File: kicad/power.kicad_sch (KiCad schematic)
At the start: 18 parts, among them J13 USB4125-GF-A, SW1 ANT11TFHQE, SW2 E112SD1A3QE, U40 MCP1700-3302E/TO, X1 25.175 MHz

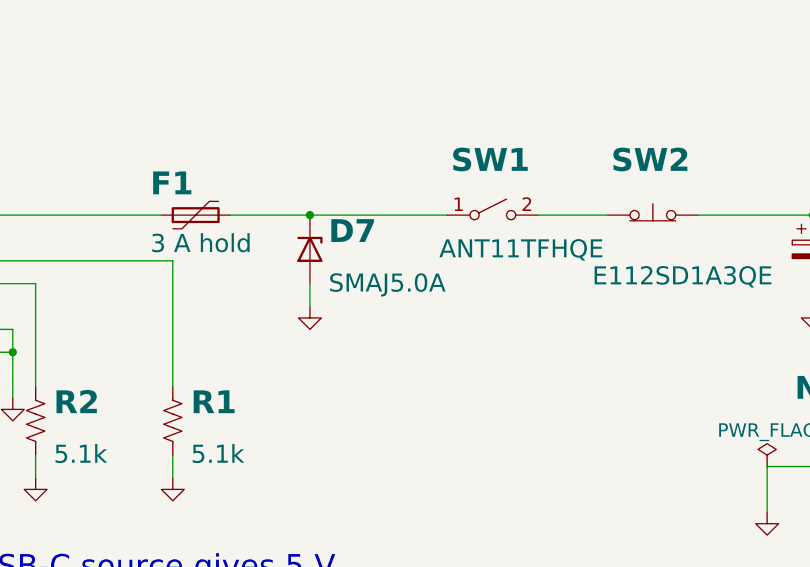
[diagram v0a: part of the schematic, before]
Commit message: Through-hole ESD clamps on external I/O; D7 TVS to through-hole SA5.0A
BAT85 steering pairs to +5V and GND on every PS/2 and SNES signal line
(D8-D21, shared port sheet) and on the VGA syncs (D22-D25, video sheet).
D7 changes from the SMD SMAJ5.0A to the DO-15 SA5.0A (through hole
wherever possible). BOM, docs and PDFs regenerated.

Co-Authored-By: Claude Opus 5.5 (1M context) <noreply@anthropic.com>
Claude-Session: https://claude.ai/code/session_01L9AkLuEg13EebxDmgXsaEp
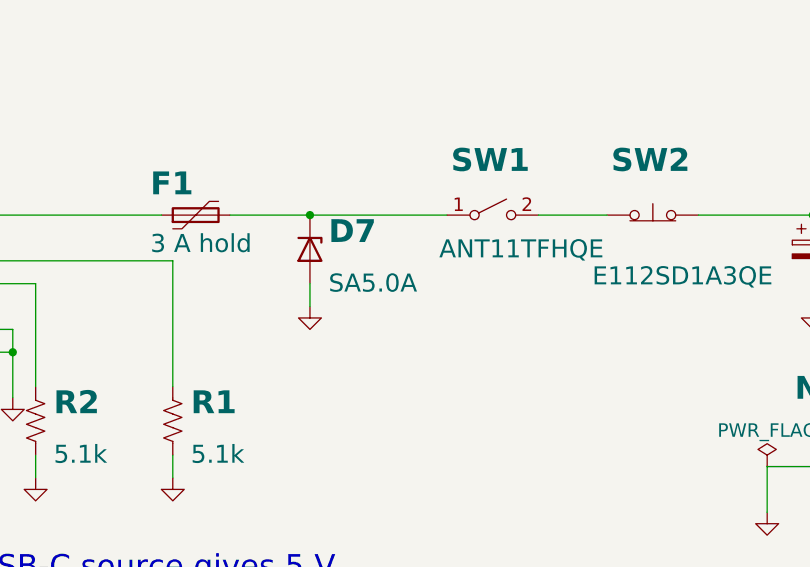
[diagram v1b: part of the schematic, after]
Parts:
- D7: value SMAJ5.0A -> SA5.0A; footprint Diode_SMD:D_SMA -> Diode_THT:D_DO-15_P10.16mm_Horizontal; MPN SMAJ5.0A -> SA5.0A
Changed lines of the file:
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@@
   (wire (pts (xy 104.14 88.9) (xy 104.14 91.44)) (stroke (width 0) (type default)))
   (symbol (lib_id "power:GND") (at 104.14 91.44 0) (unit 1) (in_bom yes) (on_board yes) (dnp no) (property "Reference" "#PWR0202" (at 104.14 91.44 0) (effects (font (size 1.27 1.27)) hide)) (property "Value" "GND" (at 104.14 97.79 0) (effects (font (size 2 2)) hide)) (property "Footprint" "" (at 104.14 91.44 0) (effects (font (size 1.27 1.27)) hide)) (property "Datasheet" "" (at 104.14 91.44 0) (effects (font (size 1.27 1.27)) hide)) (pin "1") (instances (project "placard" (path "/e3450542-4ffc-59d4-a4a7-45636233928a/f2696644-57a6-5352-a354-a3e1bf43cc65" (reference "#PWR0202") (unit 1)))))
-  (symbol (lib_id "placard_std:D_Zener") (at 104.14 85.09 270) (unit 1) (in_bom yes) (on_board yes) (dnp no) (property "Reference" "D7" (at 106.2 84.58 90) (effects (font (size 2.54 2.54) bold) (justify left bottom))) (property "Value" "SMAJ5.0A" (at 106.2 87.68 90) (effects (font (size 2 2)) (justify left top))) (property "Footprint" "Diode_SMD:D_SMA" (at 104.14 85.09 0) (effects (font (size 1.27 1.27)) hide)) (property "Datasheet" "~" (at 104.14 85.09 0) (effects (font (size 1.27 1.27)) hide)) (property "Manufacturer" "Littelfuse" (at 104.14 85.09 0) (effects (font (size 1.27 1.27)) hide)) (property "MPN" "SMAJ5.0A" (at 104.14 85.09 0) (effects (font (size 1.27 1.27)) hide)) (pin "1") (pin "2") (instances (project "placard" (path "/e3450542-4ffc-59d4-a4a7-45636233928a/f2696644-57a6-5352-a354-a3e1bf43cc65" (reference "D7") (unit 1)))))
+  (symbol (lib_id "placard_std:D_Zener") (at 104.14 85.09 270) (unit 1) (in_bom yes) (on_board yes) (dnp no) (property "Reference" "D7" (at 106.2 84.58 90) (effects (font (size 2.54 2.54) bold) (justify left bottom))) (property "Value" "SA5.0A" (at 106.2 87.68 90) (effects (font (size 2 2)) (justify left top))) (property "Footprint" "Diode_THT:D_DO-15_P10.16mm_Horizontal" (at 104.14 85.09 0) (effects (font (size 1.27 1.27)) hide)) (property "Datasheet" "~" (at 104.14 85.09 0) (effects (font (size 1.27 1.27)) hide)) (property "Manufacturer" "Littelfuse" (at 104.14 85.09 0) (effects (font (size 1.27 1.27)) hide)) (property "MPN" "SA5.0A" (at 104.14 85.09 0) (effects (font (size 1.27 1.27)) hide)) (pin "1") (pin "2") (instances (project "placard" (path "/e3450542-4ffc-59d4-a4a7-45636233928a/f2696644-57a6-5352-a354-a3e1bf43cc65" (reference "D7") (unit 1)))))
   (wire (pts (xy 95.25 81.28) (xy 104.14 81.28)) (stroke (width 0) (type default)))
   (wire (pts (xy 104.14 81.28) (xy 119.38 81.28)) (stroke (width 0) (type default)))

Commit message: Part numbers for the remaining parts; J6 Tensility 54-00174; optional J1 and J9-J12
Every schematic part gets Manufacturer/MPN: Yageo MFR-25 resistors by value,
Bourns 4609X networks, KEMET/TDK ceramics, Panasonic FR electrolytics, ECS
oscillator, Assmann VGA, Sullins headers, Wurth box header, Cherry switches.
Sockets get On Shore numbers (0.3" 24/28-pin are ED241DT/ED281DT; ED28DT is
0.6"). J6 becomes the Tensility 54-00174 TRRS jack with a footprint drawn
from its datasheet. Digi-Key prices from Justin for the oscillator, VGA and
audio jack. The expansion slot sockets and the keyboard header are optional,
with a BOM total without them.

Co-Authored-By: Claude Opus 5.5 (1M context) <noreply@anthropic.com>
Claude-Session: https://claude.ai/code/session_01L9AkLuEg13EebxDmgXsaEp
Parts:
- C40, C42: MPN (none) -> C330C105K5R5TA; Manufacturer (none) -> KEMET
- C41: MPN (none) -> EEU-FR1E221; Manufacturer (none) -> Panasonic
- C43: MPN (none) -> C320C104K5R5TA; Manufacturer (none) -> KEMET
- JP1, JP2: MPN (none) -> PREC002SAAN-RC; Manufacturer (none) -> Sullins
- R1, R2: MPN (none) -> MFR-25FBF52-5K1; Manufacturer (none) -> Yageo
- R3, R4: MPN (none) -> MFR-25FBF52-10K; Manufacturer (none) -> Yageo
- X1: MPN (none) -> ECS-100A-251.7; Manufacturer (none) -> ECS Inc.

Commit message: Reset via relay: K1 G5LE-1 NC contact carries 5 V, tactile SW2 drives the coil
SW2 (C&K PTS645VL58-2 LFS) pulls in K1 (Omron G5LE-1 DC5) from VON, so
holding it opens the 5 V line; D26 (BAT85) across the coil. Replaces the
4 A E112SD1A3QE (about $11 -> $2). C41 moves ahead of K1 onto VON so the
board side drains faster on reset. Footprint, layout, BOM and docs updated.

Co-Authored-By: Claude Opus 5.5 (1M context) <noreply@anthropic.com>
Claude-Session: https://claude.ai/code/session_01L9AkLuEg13EebxDmgXsaEp
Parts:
- removed SW2: E112SD1A3QE, placard:SW_Push_CK_E112SD1A3QE, symbol placard_std:SW_Push_Open
- added D26: BAT85, Diode_THT:D_DO-35_SOD27_P7.62mm_Horizontal, symbol placard_std:D_Schottky
- added K1: G5LE-1 DC5, Relay_THT:Relay_SPDT_Omron-G5LE-1, symbol placard_std:G5LE-1
- added SW2: PTS645VL58-2 LFS, Button_Switch_THT:SW_Tactile_SPST_Angled_PTS645Vx58-2LFS, symbol placard_std:SW_Push
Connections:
- net +5V: now also K1.4; no longer C41.1
- net GND: now also D26.2 (A), K1.5
- net at SW1.2 (B): now also C41.1, K1.1, SW2.1
- new net: D26.1 (K), K1.2, SW2.2
- no-connect marks 0 -> 1
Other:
- note added: "one throw. SW2 reset: holding it pulls in K1,"
- note added: "whose NC contact opens the 5 V line."
- note removed: "one throw. SW2 reset: momentary, common + NC,"
- note removed: "so holding it cuts the power."

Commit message: J13: USB4125 footprint with longer SMD pads for hand soldering
New placard:USB_C_Receptacle_GCT_USB4125_6P_HandSolder, made by
gen_kicad_connectors.py from KiCad's USB4125 footprint with the six SMD
pads lengthened 1.5 mm away from the board edge (inner ends unchanged),
so the iron has room to touch each pad. Symbol, power sheet and board
now use it; board drawings regenerated.

Co-Authored-By: Claude Opus 5.5 (1M context) <noreply@anthropic.com>
Claude-Session: https://claude.ai/code/session_01SPs5Hx9ixxAAqtEGqiE4Ba
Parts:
- J13: footprint Connector_USB:USB_C_Receptacle_GCT_USB4125-xx-x_6P_TopMnt_Horizontal -> placard:USB_C_Receptacle_GCT_USB4125_6P_HandSolder
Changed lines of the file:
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@@
   (text "Power and clock" (at 15 22 0) (effects (font (size 6 6) bold) (justify left bottom)))
   (text "USB-C 5 V in, 3.3 V for the SD card, 25.175 MHz oscillator (CLK), cartridge STALL and RUN" (at 15 30 0) (effects (font (size 3 3)) (justify left bottom)))
-  (symbol (lib_id "placard_parts:USB_C_Power") (at 50.8 88.9 0) (unit 1) (in_bom yes) (on_board yes) (dnp no) (property "Reference" "J13" (at 36 75 0) (effects (font (size 2.54 2.54) bold) (justify left bottom))) (property "Value" "USB4125-GF-A" (at 36 104 0) (effects (font (size 2 2)) (justify left top))) (property "Footprint" "Connector_USB:USB_C_Receptacle_GCT_USB4125-xx-x_6P_TopMnt_Horizontal" (at 50.8 88.9 0) (effects (font (size 1.27 1.27)) hide)) (property "Datasheet" "~" (at 50.8 88.9 0) (effects (font (size 1.27 1.27)) hide)) (property "Manufacturer" "GCT" (at 50.8 88.9 0) (effects (font (size 1.27 1.27)) hide)) (property "MPN" "USB4125-GF-A" (at 50.8 88.9 0) (effects (font (size 1.27 1.27)) hide)) (pin "A9") (pin "B9") (pin "A5") (pin "B5") (pin "A12") (pin "B12") (pin "S1") (instances (project "placard" (path "/e3450542-4ffc-59d4-a4a7-45636233928a/f2696644-57a6-5352-a354-a3e1bf43cc65" (reference "J13") (unit 1)))))
+  (symbol (lib_id "placard_parts:USB_C_Power") (at 50.8 88.9 0) (unit 1) (in_bom yes) (on_board yes) (dnp no) (property "Reference" "J13" (at 36 75 0) (effects (font (size 2.54 2.54) bold) (justify left bottom))) (property "Value" "USB4125-GF-A" (at 36 104 0) (effects (font (size 2 2)) (justify left top))) (property "Footprint" "placard:USB_C_Receptacle_GCT_USB4125_6P_HandSolder" (at 50.8 88.9 0) (effects (font (size 1.27 1.27)) hide)) (property "Datasheet" "~" (at 50.8 88.9 0) (effects (font (size 1.27 1.27)) hide)) (property "Manufacturer" "GCT" (at 50.8 88.9 0) (effects (font (size 1.27 1.27)) hide)) (property "MPN" "USB4125-GF-A" (at 50.8 88.9 0) (effects (font (size 1.27 1.27)) hide)) (pin "A9") (pin "B9") (pin "A5") (pin "B5") (pin "A12") (pin "B12") (pin "S1") (instances (project "placard" (path "/e3450542-4ffc-59d4-a4a7-45636233928a/f2696644-57a6-5352-a354-a3e1bf43cc65" (reference "J13") (unit 1)))))
   (wire (pts (xy 68.58 93.98) (xy 71.12 93.98)) (stroke (width 0) (type default)))
   (wire (pts (xy 71.12 93.98) (xy 71.12 96.52)) (stroke (width 0) (type default)))

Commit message: Kit footprints: DIP sockets with puller room and part number, resistors with value
Justin: put the chip-puller room in the socket footprints (User.Eco1,
2.5 mm past each end) and the part number in silkscreen between the pin
rows; resistors get their value in silkscreen on the body. New
gen_kicad_kit_footprints.py derives them from KiCad's stock footprints;
schematic, symbols, BOM and PDFs now name them. The board file is left
as is (Justin is editing it): Update PCB from Schematic swaps them in.

Co-Authored-By: Claude Opus 5.5 (1M context) <noreply@anthropic.com>
Claude-Session: https://claude.ai/code/session_01JnVuvUvdWezUUU6Sgmg16H
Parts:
- R1, R2, R3, R4: footprint Resistor_THT:R_Axial_DIN0207_L6.3mm_D2.5mm_P10.16mm_Horizontal -> placard:R_Axial_DIN0207_L6.3mm_D2.5mm_P10.16mm_Horizontal_Value

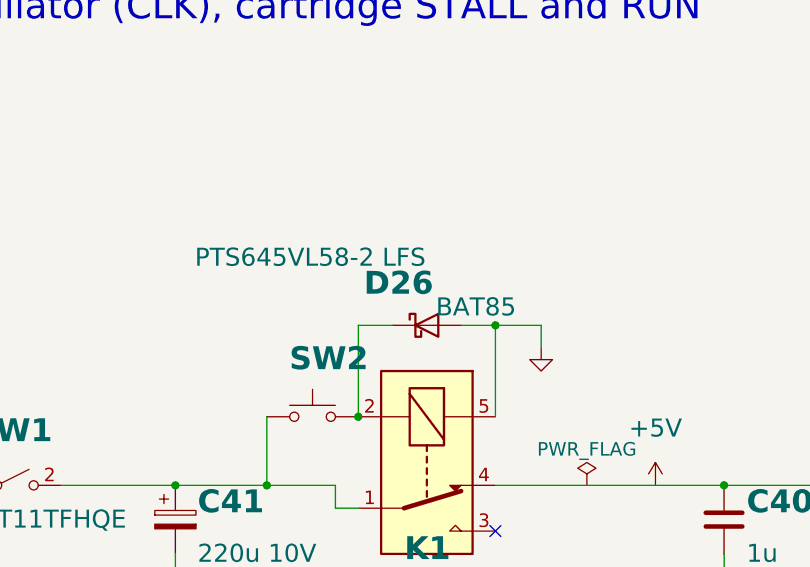
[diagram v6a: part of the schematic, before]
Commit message: Remove the ESD clamps from PS/2, SNES and VGA
Justin decided to take the BAT85 steering pairs out entirely: D8-D21
(shared port sheet) and D22-D25 (video sheet sync lines), 18 diodes.
D7 (TVS on VBUS) stays.

The remaining diodes are renumbered so every kind is numbered from 1 with
no gaps: D26 -> D8 (relay coil), D27-D29 -> D9-D11 (tint BAT85),
D30-D35 -> D12-D17 (tint 1N4148).

The schematic generator now keeps each symbol's uuid from the files
already on disk (and RENUMBERED carries a renamed part's old uuid for one
run), so Update PCB from Schematic renames the renumbered footprints and
leaves every other footprint linked.  kicad/placard.kicad_pcb is not
touched.  BOM, PDFs (no bookmarks panel), placement lists and docs updated.

Co-Authored-By: Claude Opus 5.5 (1M context) <noreply@anthropic.com>
Claude-Session: https://claude.ai/code/session_01DRvpu48w1PN7avX3eFSFuQ
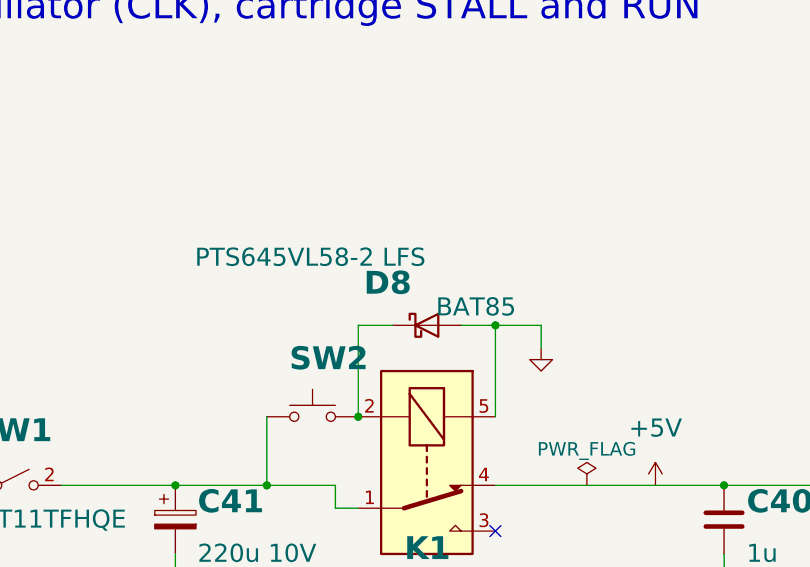
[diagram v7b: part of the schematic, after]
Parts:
- renumbered D26 to D8
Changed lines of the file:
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@@
   (symbol (lib_id "placard_std:G5LE-1") (at 170.18 78.74 270) (unit 1) (in_bom yes) (on_board yes) (dnp no) (property "Reference" "K1" (at 167.68 89.78 90) (effects (font (size 2.54 2.54) bold) (justify left bottom))) (property "Value" "G5LE-1 DC5" (at 167.68 92.28 90) (effects (font (size 2 2)) (justify left top))) (property "Footprint" "Relay_THT:Relay_SPDT_Omron-G5LE-1" (at 170.18 78.74 0) (effects (font (size 1.27 1.27)) hide)) (property "Datasheet" "http://www.omron.com/ecb/products/pdf/en-g5le.pdf" (at 170.18 78.74 0) (effects (font (size 1.27 1.27)) hide)) (property "Manufacturer" "Omron" (at 170.18 78.74 0) (effects (font (size 1.27 1.27)) hide)) (property "MPN" "G5LE-1 DC5" (at 170.18 78.74 0) (effects (font (size 1.27 1.27)) hide)) (pin "1") (pin "2") (pin "3") (pin "4") (pin "5") (instances (project "placard" (path "/e3450542-4ffc-59d4-a4a7-45636233928a/f2696644-57a6-5352-a354-a3e1bf43cc65" (reference "K1") (unit 1)))))
   (symbol (lib_id "placard_std:SW_Push") (at 157.48 73.66 0) (unit 1) (in_bom yes) (on_board yes) (dnp no) (property "Reference" "SW2" (at 154.9 68.68 0) (effects (font (size 2.54 2.54) bold) (justify left bottom))) (property "Value" "PTS645VL58-2 LFS" (at 144.4 54.78 0) (effects (font (size 2 2)) (justify left top))) (property "Footprint" "Button_Switch_THT:SW_Tactile_SPST_Angled_PTS645Vx58-2LFS" (at 157.48 73.66 0) (effects (font (size 1.27 1.27)) hide)) (property "Datasheet" "~" (at 157.48 73.66 0) (effects (font (size 1.27 1.27)) hide)) (property "Manufacturer" "C&K" (at 157.48 73.66 0) (effects (font (size 1.27 1.27)) hide)) (property "MPN" "PTS645VL58-2 LFS" (at 157.48 73.66 0) (effects (font (size 1.27 1.27)) hide)) (pin "1") (pin "2") (instances (project "placard" (path "/e3450542-4ffc-59d4-a4a7-45636233928a/f2696644-57a6-5352-a354-a3e1bf43cc65" (reference "SW2") (unit 1)))))
-  (symbol (lib_id "placard_std:D_Schottky") (at 170.18 63.5 0) (unit 1) (in_bom yes) (on_board yes) (dnp no) (property "Reference" "D26" (at 163.18 60.3 0) (effects (font (size 2.54 2.54) bold) (justify left bottom))) (property "Value" "BAT85" (at 171.18 60.3 0) (effects (font (size 2 2)) (justify left top))) (property "Footprint" "Diode_THT:D_DO-35_SOD27_P7.62mm_Horizontal" (at 170.18 63.5 0) (effects (font (size 1.27 1.27)) hide)) (property "Datasheet" "~" (at 170.18 63.5 0) (effects (font (size 1.27 1.27)) hide)) (property "Manufacturer" "Vishay" (at 170.18 63.5 0) (effects (font (size 1.27 1.27)) hide)) (property "MPN" "BAT85" (at 170.18 63.5 0) (effects (font (size 1.27 1.27)) hide)) (pin "1") (pin "2") (instances (project "placard" (path "/e3450542-4ffc-59d4-a4a7-45636233928a/f2696644-57a6-5352-a354-a3e1bf43cc65" (reference "D26") (unit 1)))))
+  (symbol (lib_id "placard_std:D_Schottky") (at 170.18 63.5 0) (unit 1) (in_bom yes) (on_board yes) (dnp no) (property "Reference" "D8" (at 163.18 60.3 0) (effects (font (size 2.54 2.54) bold) (justify left bottom))) (property "Value" "BAT85" (at 171.18 60.3 0) (effects (font (size 2 2)) (justify left top))) (property "Footprint" "Diode_THT:D_DO-35_SOD27_P7.62mm_Horizontal" (at 170.18 63.5 0) (effects (font (size 1.27 1.27)) hide)) (property "Datasheet" "~" (at 170.18 63.5 0) (effects (font (size 1.27 1.27)) hide)) (property "Manufacturer" "Vishay" (at 170.18 63.5 0) (effects (font (size 1.27 1.27)) hide)) (property "MPN" "BAT85" (at 170.18 63.5 0) (effects (font (size 1.27 1.27)) hide)) (pin "1") (pin "2") (instances (project "placard" (path "/e3450542-4ffc-59d4-a4a7-45636233928a/f2696644-57a6-5352-a354-a3e1bf43cc65" (reference "D8") (unit 1)))))
   (wire (pts (xy 142.24 88.9) (xy 142.24 91.44)) (stroke (width 0) (type default)))
   (symbol (lib_id "power:GND") (at 142.24 91.44 0) (unit 1) (in_bom yes) (on_board yes) (dnp no) (property "Reference" "#PWR0203" (at 142.24 91.44 0) (effects (font (size 1.27 1.27)) hide)) (property "Value" "GND" (at 142.24 97.79 0) (effects (font (size 2 2)) hide)) (property "Footprint" "" (at 142.24 91.44 0) (effects (font (size 1.27 1.27)) hide)) (property "Datasheet" "" (at 142.24 91.44 0) (effects (font (size 1.27 1.27)) hide)) (pin "1") (instances (project "placard" (path "/e3450542-4ffc-59d4-a4a7-45636233928a/f2696644-57a6-5352-a354-a3e1bf43cc65" (reference "#PWR0203") (unit 1)))))
